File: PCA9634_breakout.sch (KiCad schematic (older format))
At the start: 26 parts, among them J1 Conn_01x05_Male, U1 PCA9634PW_118

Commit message: feat: Changed footprints such that they are featured in the JLCPCB SMT assembly service as basic parts.
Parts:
- C1: value 47uF -> 10uF; footprint Capacitor_Tantalum_SMD:CP_EIA-3528-12_Kemet-T_Pad1.50x2.35mm_HandSolder -> Capacitor_Tantalum_SMD:CP_EIA-3216-18_Kemet-A; JLCPCB (none) -> C7171
- D1: footprint LED_SMD:LED_1206_3216Metric_Pad1.42x1.75mm_HandSolder -> LED_SMD:LED_0805_2012Metric_Castellated; JLCPCB (none) -> C2296
- D2, D3, D4, D5, D6, D7, D8: footprint LED_SMD:LED_1206_3216Metric_Pad1.42x1.75mm_HandSolder -> LED_SMD:LED_0805_2012Metric_Castellated
- R1: value 220 -> 150; footprint Resistor_SMD:R_1206_3216Metric_Pad1.30x1.75mm_HandSolder -> Resistor_SMD:R_0805_2012Metric; JLCPCB (none) -> C17471
- R2, R3, R4, R5, R6, R7, R8: value 220 -> 150; footprint Resistor_SMD:R_1206_3216Metric_Pad1.30x1.75mm_HandSolder -> Resistor_SMD:R_0805_2012Metric
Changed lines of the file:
@@
 F 0 "D1" V 5589 2082 50  0000 R CNN
 F 1 "LED" V 5498 2082 50  0000 R CNN
-F 2 "LED_SMD:LED_1206_3216Metric_Pad1.42x1.75mm_HandSolder" H 5550 2200 50  0001 C CNN
+F 2 "LED_SMD:LED_0805_2012Metric_Castellated" H 5550 2200 50  0001 C CNN
 F 3 "~" H 5550 2200 50  0001 C CNN
+F 4 "C2296" V 5550 2200 50  0001 C CNN "JLCPCB"
 	1    5550 2200
 	0    -1   -1   0
@@
 P 5550 2700
 F 0 "R1" H 5620 2746 50  0000 L CNN
-F 1 "220" H 5620 2655 50  0000 L CNN
-F 2 "Resistor_SMD:R_1206_3216Metric_Pad1.30x1.75mm_HandSolder" V 5480 2700 50  0001 C CNN
+F 1 "150" H 5620 2655 50  0000 L CNN
+F 2 "Resistor_SMD:R_0805_2012Metric" V 5480 2700 50  0001 C CNN
 F 3 "~" H 5550 2700 50  0001 C CNN
+F 4 "C17471" H 5550 2700 50  0001 C CNN "JLCPCB"
 	1    5550 2700
 	1    0    0    -1
@@
 F 0 "D2" V 6089 2082 50  0000 R CNN
 F 1 "LED" V 5998 2082 50  0000 R CNN
-F 2 "LED_SMD:LED_1206_3216Metric_Pad1.42x1.75mm_HandSolder" H 6050 2200 50  0001 C CNN
+F 2 "LED_SMD:LED_0805_2012Metric_Castellated" H 6050 2200 50  0001 C CNN
 F 3 "~" H 6050 2200 50  0001 C CNN
 	1    6050 2200
@@
 P 6050 2700
 F 0 "R2" H 6120 2746 50  0000 L CNN
-F 1 "220" H 6120 2655 50  0000 L CNN
-F 2 "Resistor_SMD:R_1206_3216Metric_Pad1.30x1.75mm_HandSolder" V 5980 2700 50  0001 C CNN
+F 1 "150" H 6120 2655 50  0000 L CNN
+F 2 "Resistor_SMD:R_0805_2012Metric" V 5980 2700 50  0001 C CNN
 F 3 "~" H 6050 2700 50  0001 C CNN
 	1    6050 2700
@@
 F 0 "D3" V 6589 2082 50  0000 R CNN
 F 1 "LED" V 6498 2082 50  0000 R CNN
-F 2 "LED_SMD:LED_1206_3216Metric_Pad1.42x1.75mm_HandSolder" H 6550 2200 50  0001 C CNN
+F 2 "LED_SMD:LED_0805_2012Metric_Castellated" H 6550 2200 50  0001 C CNN
 F 3 "~" H 6550 2200 50  0001 C CNN
 	1    6550 2200
@@
 P 6550 2700
 F 0 "R3" H 6620 2746 50  0000 L CNN
-F 1 "220" H 6620 2655 50  0000 L CNN
-F 2 "Resistor_SMD:R_1206_3216Metric_Pad1.30x1.75mm_HandSolder" V 6480 2700 50  0001 C CNN
+F 1 "150" H 6620 2655 50  0000 L CNN
+F 2 "Resistor_SMD:R_0805_2012Metric" V 6480 2700 50  0001 C CNN
 F 3 "~" H 6550 2700 50  0001 C CNN
 	1    6550 2700
@@
 F 0 "D4" V 7089 2082 50  0000 R CNN
 F 1 "LED" V 6998 2082 50  0000 R CNN
-F 2 "LED_SMD:LED_1206_3216Metric_Pad1.42x1.75mm_HandSolder" H 7050 2200 50  0001 C CNN
+F 2 "LED_SMD:LED_0805_2012Metric_Castellated" H 7050 2200 50  0001 C CNN
 F 3 "~" H 7050 2200 50  0001 C CNN
 	1    7050 2200
@@
 P 7050 2700
 F 0 "R4" H 7120 2746 50  0000 L CNN
-F 1 "220" H 7120 2655 50  0000 L CNN
-F 2 "Resistor_SMD:R_1206_3216Metric_Pad1.30x1.75mm_HandSolder" V 6980 2700 50  0001 C CNN
+F 1 "150" H 7120 2655 50  0000 L CNN
+F 2 "Resistor_SMD:R_0805_2012Metric" V 6980 2700 50  0001 C CNN
 F 3 "~" H 7050 2700 50  0001 C CNN
 	1    7050 2700
@@
 F 0 "D5" V 7589 2082 50  0000 R CNN
 F 1 "LED" V 7498 2082 50  0000 R CNN
-F 2 "LED_SMD:LED_1206_3216Metric_Pad1.42x1.75mm_HandSolder" H 7550 2200 50  0001 C CNN
+F 2 "LED_SMD:LED_0805_2012Metric_Castellated" H 7550 2200 50  0001 C CNN
 F 3 "~" H 7550 2200 50  0001 C CNN
 	1    7550 2200
@@
 P 7550 2700
 F 0 "R5" H 7620 2746 50  0000 L CNN
-F 1 "220" H 7620 2655 50  0000 L CNN
-F 2 "Resistor_SMD:R_1206_3216Metric_Pad1.30x1.75mm_HandSolder" V 7480 2700 50  0001 C CNN
+F 1 "150" H 7620 2655 50  0000 L CNN
+F 2 "Resistor_SMD:R_0805_2012Metric" V 7480 2700 50  0001 C CNN
 F 3 "~" H 7550 2700 50  0001 C CNN
 	1    7550 2700
@@
 F 0 "D6" V 8089 2082 50  0000 R CNN
 F 1 "LED" V 7998 2082 50  0000 R CNN
-F 2 "LED_SMD:LED_1206_3216Metric_Pad1.42x1.75mm_HandSolder" H 8050 2200 50  0001 C CNN
+F 2 "LED_SMD:LED_0805_2012Metric_Castellated" H 8050 2200 50  0001 C CNN
 F 3 "~" H 8050 2200 50  0001 C CNN
 	1    8050 2200
@@
 P 8050 2700
 F 0 "R6" H 8120 2746 50  0000 L CNN
-F 1 "220" H 8120 2655 50  0000 L CNN
-F 2 "Resistor_SMD:R_1206_3216Metric_Pad1.30x1.75mm_HandSolder" V 7980 2700 50  0001 C CNN
+F 1 "150" H 8120 2655 50  0000 L CNN
+F 2 "Resistor_SMD:R_0805_2012Metric" V 7980 2700 50  0001 C CNN
 F 3 "~" H 8050 2700 50  0001 C CNN
 	1    8050 2700
@@
 F 0 "D7" V 8589 2082 50  0000 R CNN
 F 1 "LED" V 8498 2082 50  0000 R CNN
-F 2 "LED_SMD:LED_1206_3216Metric_Pad1.42x1.75mm_HandSolder" H 8550 2200 50  0001 C CNN
+F 2 "LED_SMD:LED_0805_2012Metric_Castellated" H 8550 2200 50  0001 C CNN
 F 3 "~" H 8550 2200 50  0001 C CNN
 	1    8550 2200
@@
 P 8550 2700
 F 0 "R7" H 8620 2746 50  0000 L CNN
-F 1 "220" H 8620 2655 50  0000 L CNN
-F 2 "Resistor_SMD:R_1206_3216Metric_Pad1.30x1.75mm_HandSolder" V 8480 2700 50  0001 C CNN
+F 1 "150" H 8620 2655 50  0000 L CNN
+F 2 "Resistor_SMD:R_0805_2012Metric" V 8480 2700 50  0001 C CNN
 F 3 "~" H 8550 2700 50  0001 C CNN
 	1    8550 2700
@@
 F 0 "D8" V 9089 2082 50  0000 R CNN
 F 1 "LED" V 8998 2082 50  0000 R CNN
-F 2 "LED_SMD:LED_1206_3216Metric_Pad1.42x1.75mm_HandSolder" H 9050 2200 50  0001 C CNN
+F 2 "LED_SMD:LED_0805_2012Metric_Castellated" H 9050 2200 50  0001 C CNN
 F 3 "~" H 9050 2200 50  0001 C CNN
 	1    9050 2200
@@
 P 9050 2700
 F 0 "R8" H 9120 2746 50  0000 L CNN
-F 1 "220" H 9120 2655 50  0000 L CNN
-F 2 "Resistor_SMD:R_1206_3216Metric_Pad1.30x1.75mm_HandSolder" V 8980 2700 50  0001 C CNN
+F 1 "150" H 9120 2655 50  0000 L CNN
+F 2 "Resistor_SMD:R_0805_2012Metric" V 8980 2700 50  0001 C CNN
 F 3 "~" H 9050 2700 50  0001 C CNN
 	1    9050 2700
@@
 P 6300 6450
 F 0 "C1" H 6418 6496 50  0000 L CNN
-F 1 "47uF" H 6418 6405 50  0000 L CNN
-F 2 "Capacitor_Tantalum_SMD:CP_EIA-3528-12_Kemet-T_Pad1.50x2.35mm_HandSolder" H 6338 6300 50  0001 C CNN
+F 1 "10uF" H 6418 6405 50  0000 L CNN
+F 2 "Capacitor_Tantalum_SMD:CP_EIA-3216-18_Kemet-A" H 6338 6300 50  0001 C CNN
 F 3 "~" H 6300 6450 50  0001 C CNN
+F 4 "C7171" H 6300 6450 50  0001 C CNN "JLCPCB"
 	1    6300 6450
 	1    0    0    -1

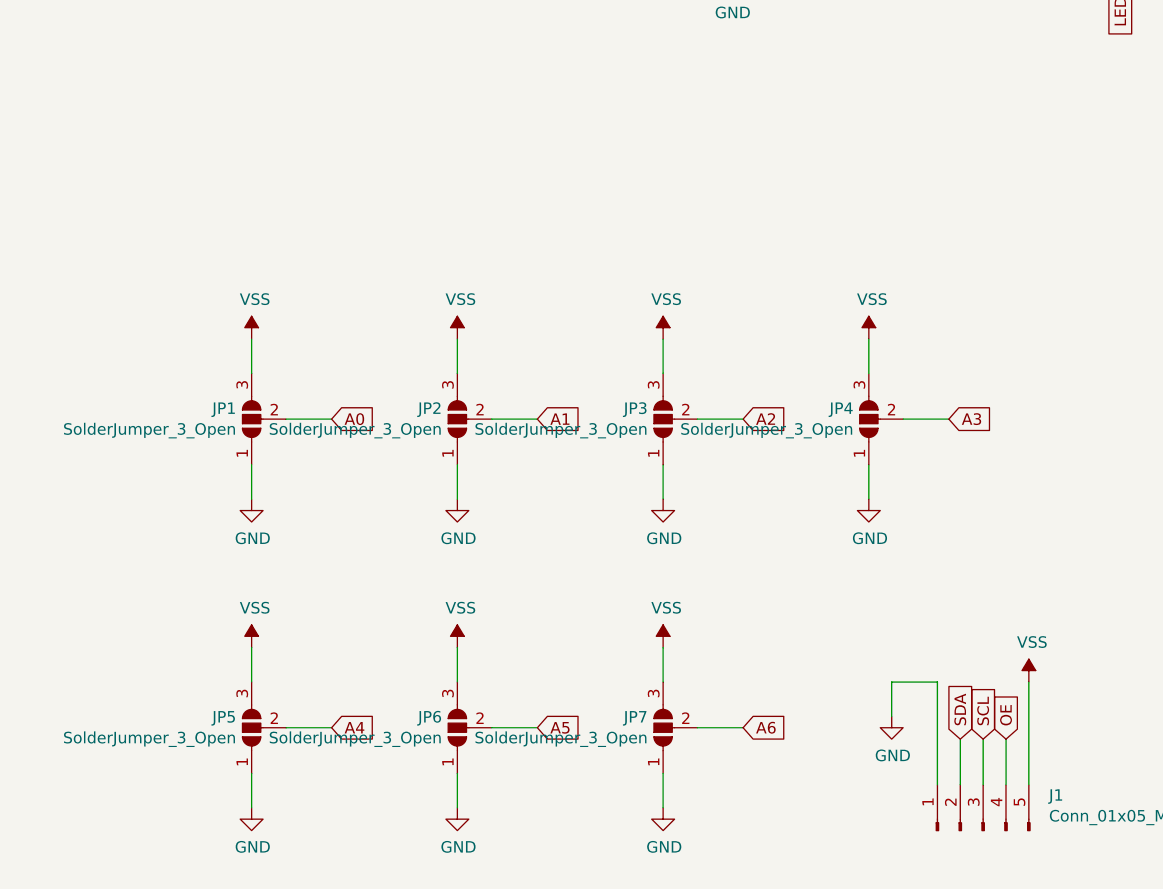
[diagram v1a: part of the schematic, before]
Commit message: changed solder jumper to double row pin 2.54 connector on top side
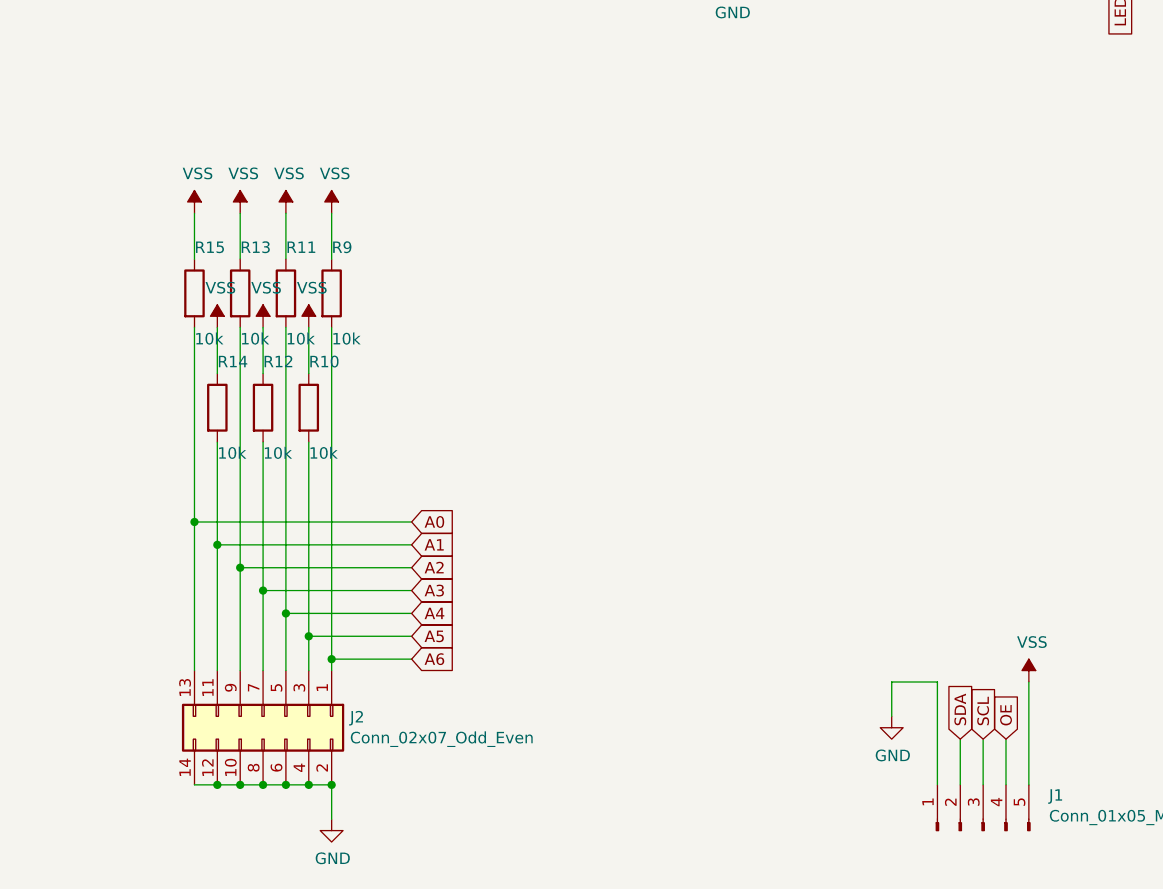
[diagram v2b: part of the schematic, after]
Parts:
- removed JP1, JP2, JP3, JP4, JP5, JP6, JP7: SolderJumper_3_Open, Jumper:SolderJumper-3_P1.3mm_Open_RoundedPad1.0x1.5mm, symbol Jumper:SolderJumper_3_Open
- added J2: Conn_02x07_Odd_Even, Connector_PinHeader_2.54mm:PinHeader_2x07_P2.54mm_Vertical, symbol Connector_Generic:Conn_02x07_Odd_Even
- added R10, R11, R12, R13, R14, R15, R9: 10k, Resistor_SMD:R_0805_2012Metric, symbol Device:R
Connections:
- net A0: now also J2.13 (Pin_13), R15.2
- net A1: now also J2.11 (Pin_11), R14.2
- net A2: now also J2.9 (Pin_9), R13.2
- net A3: now also J2.7 (Pin_7), R12.2
- net A4: now also J2.5 (Pin_5), R11.2
- net A5: now also J2.3 (Pin_3), R10.2
- net A6: now also J2.1 (Pin_1), R9.2
- net GND: now also J2.10 (Pin_10), J2.12 (Pin_12), J2.14 (Pin_14), J2.2 (Pin_2), J2.4 (Pin_4), J2.6 (Pin_6), J2.8 (Pin_8)
- net VSS: now also R10.1, R11.1, R12.1, R13.1, R14.1, R15.1, R9.1
